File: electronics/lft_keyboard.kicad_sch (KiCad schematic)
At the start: 34 parts, among them J5 Conn_01x04, J6 Conn_01x04, J7 Conn_01x04, J8 Conn_01x04, SW1 SW_SPST, SW10 SW_SPST, SW11 SW_SPST, SW12 SW_SPST, SW13 SW_SPST, SW14 SW_SPST, SW15 SW_SPST, SW16 SW_SPST, SW17 SW_SPST, SW18 SW_SPST, SW19 SW_SPST, SW2 SW_SPST, SW20 SW_SPST, SW21 SW_SPST, SW22 SW_SPST, SW23 SW_SPST, SW24 SW_SPST, SW25 SW_SPST, SW26 SW_SPST, SW27 SW_SPST, SW28 SW_SPST, SW29 SW_SPST, SW3 SW_SPST, SW4 SW_SPST, SW5 SW_SPST, SW6 SW_SPST, SW7 SW_SPST, SW8 SW_SPST, SW9 SW_SPST, U2 PCA9506DGG

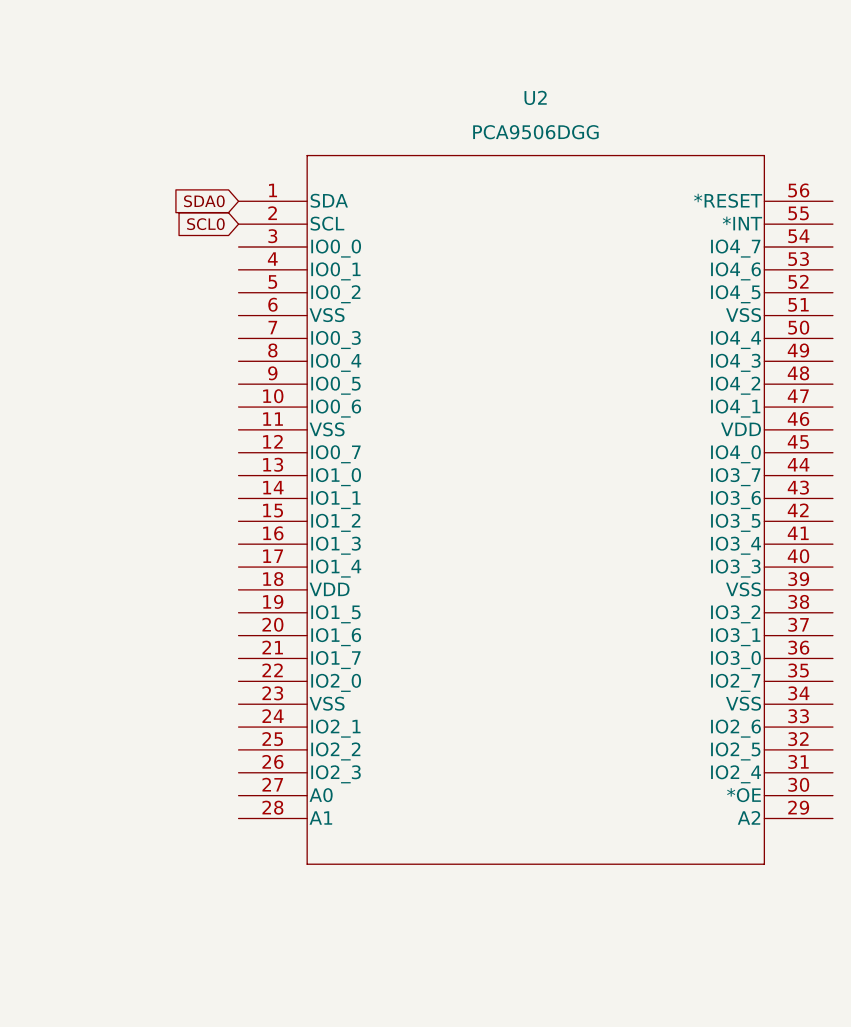
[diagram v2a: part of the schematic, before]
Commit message: change IO expander
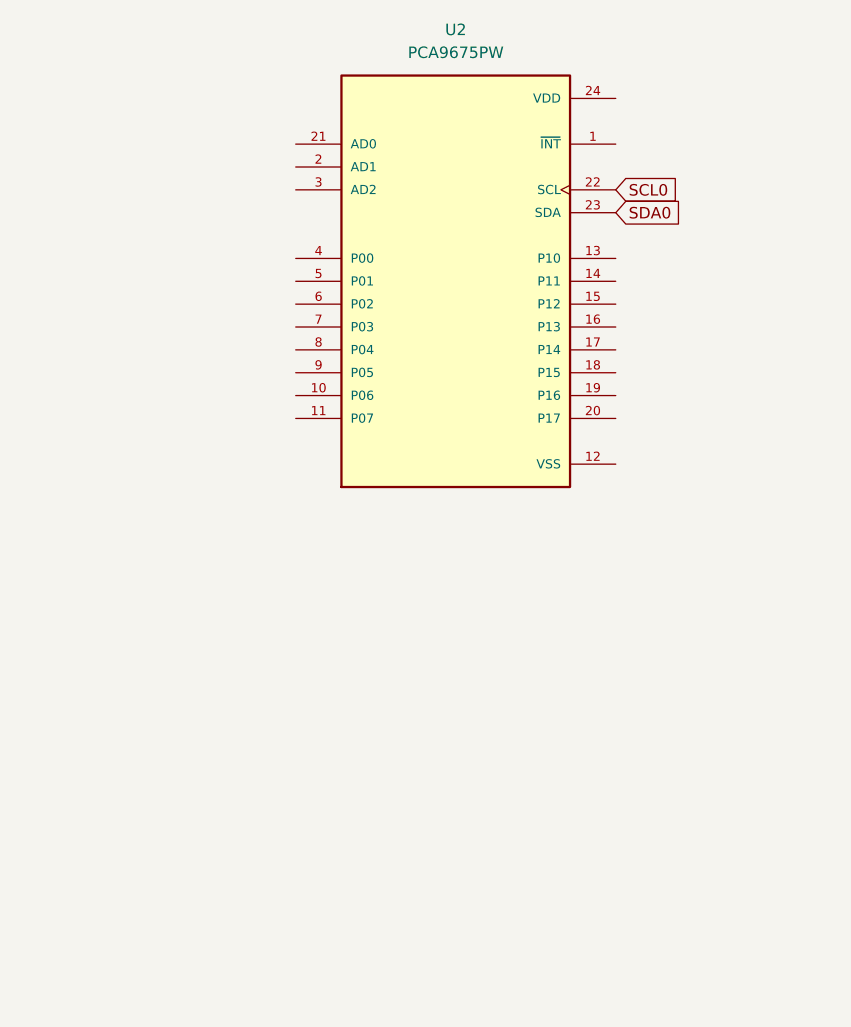
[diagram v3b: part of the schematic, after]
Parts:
- removed U2: PCA9506DGG, PCA9506:PCA9506DGG, symbol PCA9506:PCA9506DGG
- added U2: PCA9675PW, PCA9675PW:SOP65P640X110-24N, symbol PCA9675PW_118:PCA9675PW
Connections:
- net SCL0: now also U2.22 (SCL)
- net SDA0: now also U2.23 (SDA)

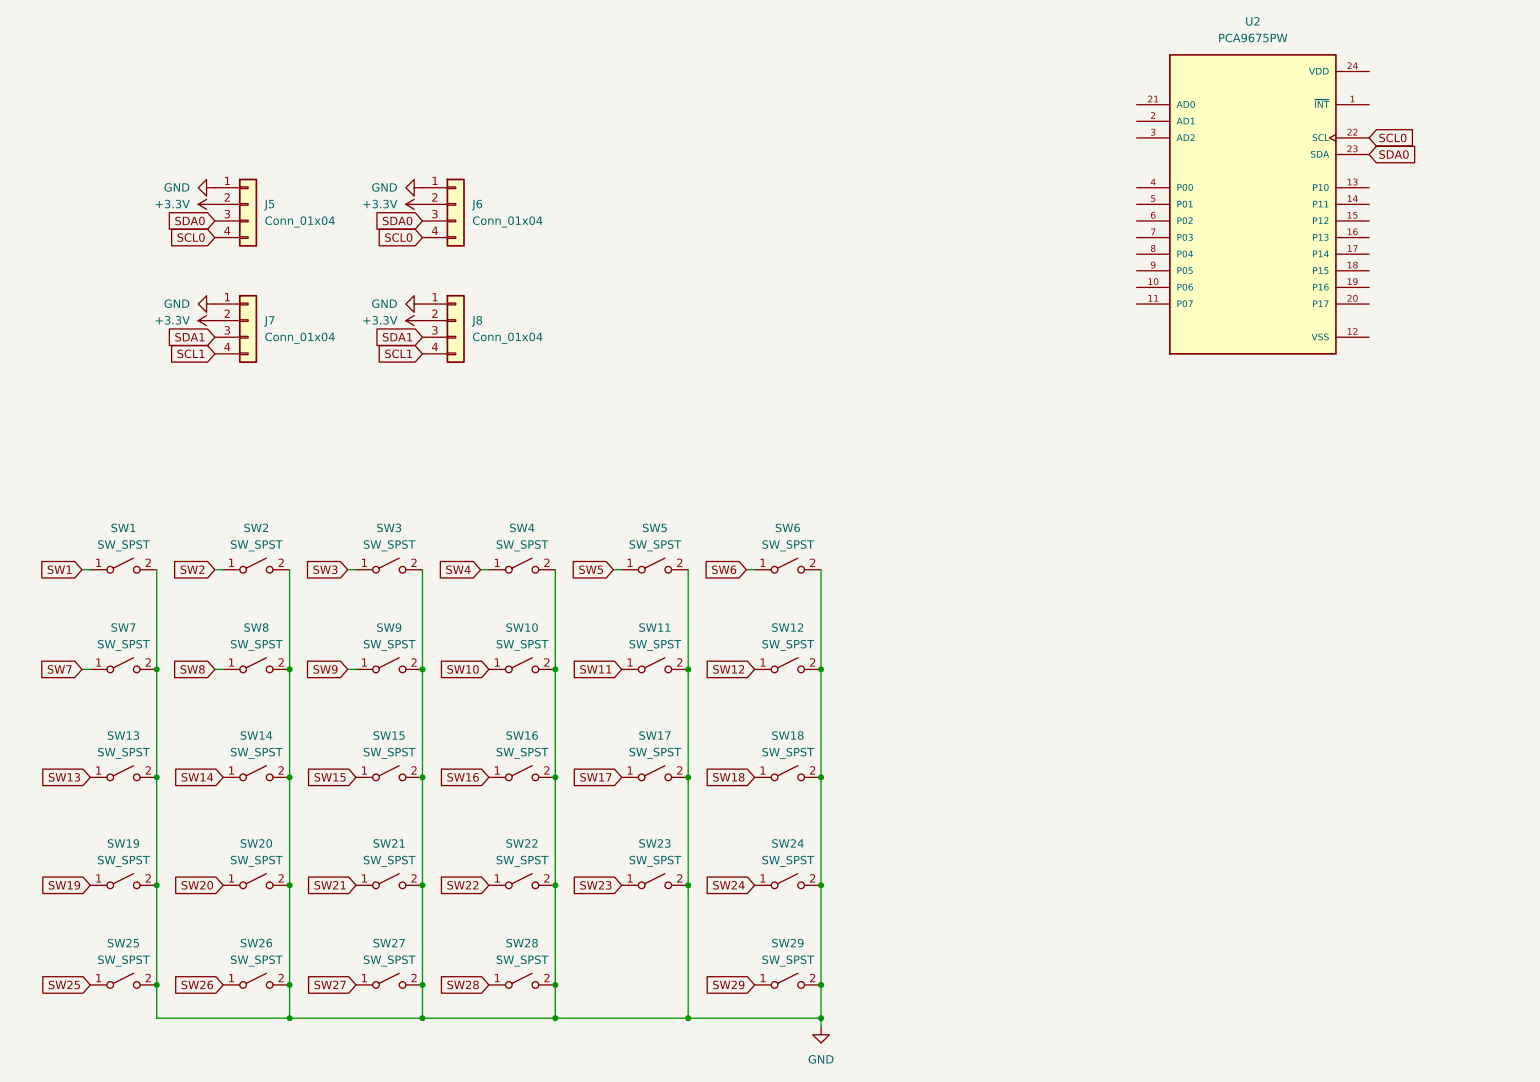
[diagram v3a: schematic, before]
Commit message: begin working on mini-matrix routing
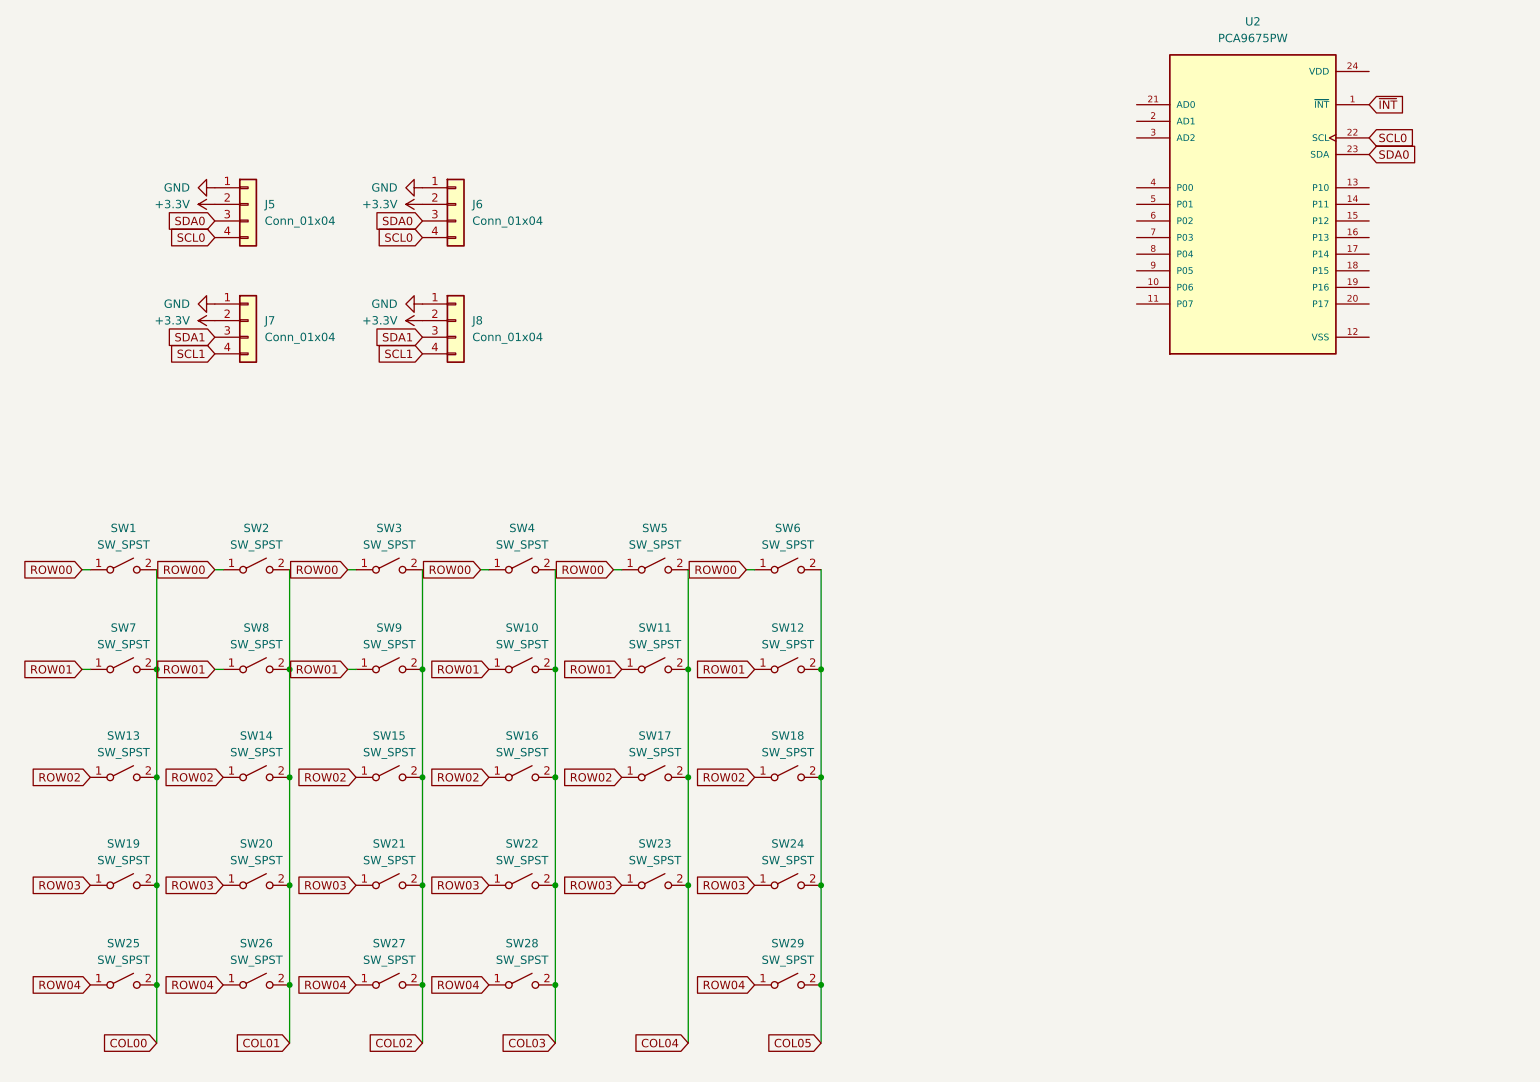
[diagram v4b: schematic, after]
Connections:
- net SW11 is gone; now on net ROW01: SW11.1 (A)
- net SW12 is gone; now on net ROW01: SW12.1 (A)
- net SW14 is gone; now on net ROW02: SW14.1 (A)
- net SW15 is gone; now on net ROW02: SW15.1 (A)
- net SW16 is gone; now on net ROW02: SW16.1 (A)
- net SW17 is gone; now on net ROW02: SW17.1 (A)
- net SW18 is gone; now on net ROW02: SW18.1 (A)
- net SW2 is gone; now on net ROW00: SW2.1 (A)
- net SW20 is gone; now on net ROW03: SW20.1 (A)
- net SW21 is gone; now on net ROW03: SW21.1 (A)
- net SW22 is gone; now on net ROW03: SW22.1 (A)
- net SW23 is gone; now on net ROW03: SW23.1 (A)
- net SW24 is gone; now on net ROW03: SW24.1 (A)
- net SW26 is gone; now on net ROW04: SW26.1 (A)
- net SW27 is gone; now on net ROW04: SW27.1 (A)
- net SW28 is gone; now on net ROW04: SW28.1 (A)
- net SW29 is gone; now on net ROW04: SW29.1 (A)
- net SW3 is gone; now on net ROW00: SW3.1 (A)
- net SW4 is gone; now on net ROW00: SW4.1 (A)
- net SW5 is gone; now on net ROW00: SW5.1 (A)
- net SW6 is gone; now on net ROW00: SW6.1 (A)
- net SW7 is gone; now on net ROW01: SW7.1 (A)
- net SW8 is gone; now on net ROW01: SW8.1 (A)
- net SW9 is gone; now on net ROW01: SW9.1 (A)
- net GND: no longer SW1.2 (B), SW10.2 (B), SW11.2 (B), SW12.2 (B), SW13.2 (B), SW14.2 (B), SW15.2 (B), SW16.2 (B), SW17.2 (B), SW18.2 (B), SW19.2 (B), SW2.2 (B), SW20.2 (B), SW21.2 (B), SW22.2 (B), SW23.2 (B), SW24.2 (B), SW25.2 (B), SW26.2 (B), SW27.2 (B), SW28.2 (B), SW29.2 (B), SW3.2 (B), SW4.2 (B), SW5.2 (B), SW6.2 (B), SW7.2 (B), SW8.2 (B), SW9.2 (B)
- net ~{INT}: now reaches U2.1 (~{INT})
- net SW1 renamed ROW00
- net SW10 renamed ROW01
- net SW13 renamed ROW02
- net SW19 renamed ROW03
- net SW25 renamed ROW04
- new net COL00: SW1.2 (B), SW13.2 (B), SW19.2 (B), SW25.2 (B), SW7.2 (B)
- new net COL01: SW14.2 (B), SW2.2 (B), SW20.2 (B), SW26.2 (B), SW8.2 (B)
- new net COL02: SW15.2 (B), SW21.2 (B), SW27.2 (B), SW3.2 (B), SW9.2 (B)
- new net COL03: SW10.2 (B), SW16.2 (B), SW22.2 (B), SW28.2 (B), SW4.2 (B)
- new net COL04: SW11.2 (B), SW17.2 (B), SW23.2 (B), SW5.2 (B)
- new net COL05: SW12.2 (B), SW18.2 (B), SW24.2 (B), SW29.2 (B), SW6.2 (B)

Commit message: begin matrix via diodes
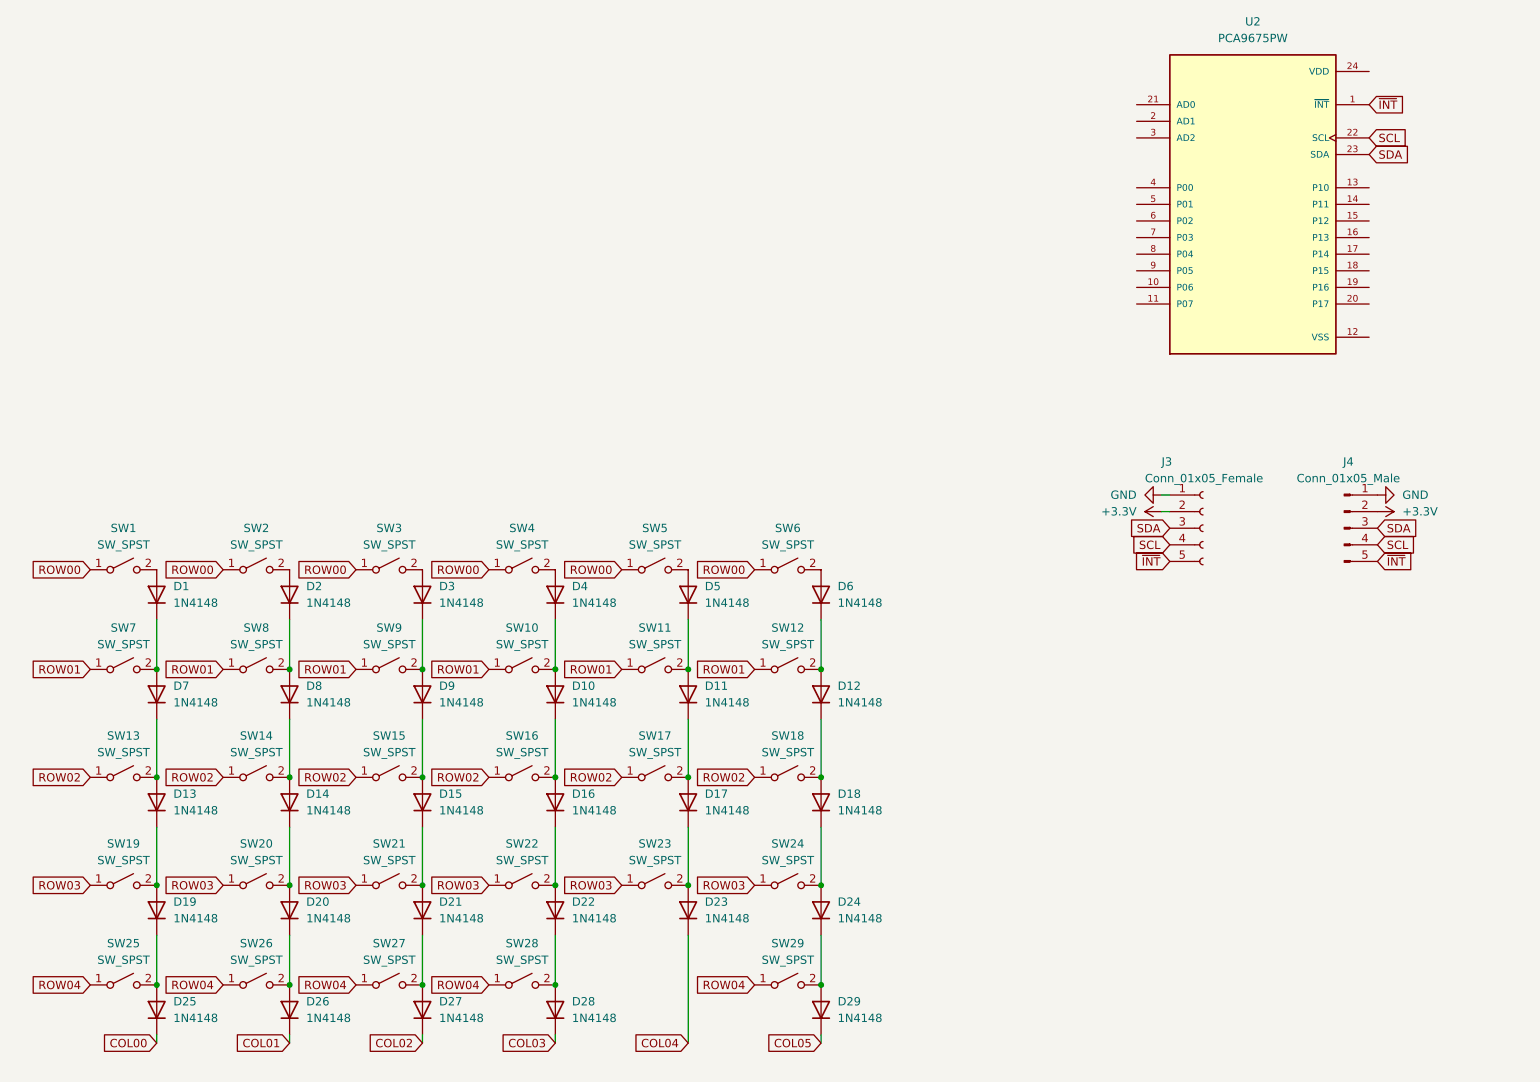
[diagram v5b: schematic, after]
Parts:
- removed J5, J6, J7, J8: Conn_01x04, symbol Connector_Generic:Conn_01x04
- added D1, D10, D11, D12, D13, D14, D15, D16, D17, D18, D19, D2, D20, D21, D22, D23, D24, D25, D26, D27, D28, D29, D3, D4, D5, D6, D7, D8, D9: 1N4148, Diode_SMD:D_SOD-123, symbol Diode:1N4148W
- added J3: Conn_01x05_Female, Connector_PinHeader_2.54mm:PinHeader_1x05_P2.54mm_Vertical, symbol Connector:Conn_01x05_Female
- added J4: Conn_01x05_Male, Connector_PinHeader_2.54mm:PinHeader_1x05_P2.54mm_Vertical, symbol Connector:Conn_01x05_Male
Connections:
- net +3V3: now also J3.2 (Pin_2), J4.2 (Pin_2)
- net COL00: now also D25.1 (K); no longer SW1.2 (B), SW13.2 (B), SW19.2 (B), SW25.2 (B), SW7.2 (B)
- net COL01: now also D26.1 (K); no longer SW14.2 (B), SW2.2 (B), SW20.2 (B), SW26.2 (B), SW8.2 (B)
- net COL02: now also D27.1 (K); no longer SW15.2 (B), SW21.2 (B), SW27.2 (B), SW3.2 (B), SW9.2 (B)
- net COL03: now also D28.1 (K); no longer SW10.2 (B), SW16.2 (B), SW22.2 (B), SW28.2 (B), SW4.2 (B)
- net COL04: now also D23.1 (K); no longer SW11.2 (B), SW17.2 (B), SW23.2 (B), SW5.2 (B)
- net COL05: now also D29.1 (K); no longer SW12.2 (B), SW18.2 (B), SW24.2 (B), SW29.2 (B), SW6.2 (B)
- net GND: now also J3.1 (Pin_1), J4.1 (Pin_1)
- net ~{INT}: now also J3.5 (Pin_5), J4.5 (Pin_5)
- net SCL0 renamed SCL
- net SCL: now also J3.4 (Pin_4), J4.4 (Pin_4)
- net SDA0 renamed SDA
- net SDA: now also J3.3 (Pin_3), J4.3 (Pin_3)
- new net: D20.1 (K), D26.2 (A), SW26.2 (B)
- new net: D14.1 (K), D20.2 (A), SW20.2 (B)
- new net: D13.2 (A), D7.1 (K), SW13.2 (B)
- new net: D22.1 (K), D28.2 (A), SW28.2 (B)
- new net: D16.1 (K), D22.2 (A), SW22.2 (B)
- new net: D24.1 (K), D29.2 (A), SW29.2 (B)
- new net: D10.2 (A), D4.1 (K), SW10.2 (B)
- new net: D4.2 (A), SW4.2 (B)
- new net: D17.1 (K), D23.2 (A), SW23.2 (B)
- new net: D18.1 (K), D24.2 (A), SW24.2 (B)
- new net: D3.1 (K), D9.2 (A), SW9.2 (B)
- new net: D3.2 (A), SW3.2 (B)
- new net: D10.1 (K), D16.2 (A), SW16.2 (B)
- new net: D19.1 (K), D25.2 (A), SW25.2 (B)
- new net: D13.1 (K), D19.2 (A), SW19.2 (B)
- new net: D1.1 (K), D7.2 (A), SW7.2 (B)
- new net: D21.1 (K), D27.2 (A), SW27.2 (B)
- new net: D15.2 (A), D9.1 (K), SW15.2 (B)
- new net: D14.2 (A), D8.1 (K), SW14.2 (B)
- new net: D2.2 (A), SW2.2 (B)
- new net: D11.2 (A), D5.1 (K), SW11.2 (B)
- new net: D11.1 (K), D17.2 (A), SW17.2 (B)
- new net: D12.1 (K), D18.2 (A), SW18.2 (B)
- new net: D12.2 (A), D6.1 (K), SW12.2 (B)
- new net: D2.1 (K), D8.2 (A), SW8.2 (B)
- new net: D15.1 (K), D21.2 (A), SW21.2 (B)
- new net: D6.2 (A), SW6.2 (B)
- new net: D1.2 (A), SW1.2 (B)
- new net: D5.2 (A), SW5.2 (B)
